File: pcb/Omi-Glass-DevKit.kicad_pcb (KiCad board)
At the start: 2 copper layers, 24.4 x 16.5 mm, 12 parts, among them J1 Conn_01x02, J2 Conn_01x02, SW1 SW_Push, U1 NCP163AFCS280T2G, U2 NCP163AFCT180T2G

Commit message: push R0.0 design for V3 glasses
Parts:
- removed the REF** at (0.00, 8.20)
- removed TH1: Thermistor_NTC, Capacitor_THT:C_Disc_D3.0mm_W1.6mm_P2.50mm
- removed U1: NCP163AFCS280T2G, Package_CSP:WLCSP-4_0.64x0.64mm_P0.35mm
- removed U2: NCP163AFCT180T2G, Package_CSP:WLCSP-4_0.64x0.64mm_P0.35mm
- added JP1: Jumper_2_Open, Jumper:SolderJumper-2_P1.3mm_Open_RoundedPad1.0x1.5mm, F.Cu at (14.3, -1.17)
- moved REF** 6.45 mm to (10.7, 2.10)
- moved J2 3.68 mm to (10.4, -4.50), turned to -90 degrees
- moved J1 2.69 mm to (13.4, -7.27)
- moved R1 0.47 mm to (11.3, 5.58)
- moved R2 0.47 mm to (11.3, 6.73)
- turned J3 to 90 degrees
- renumbered J2 to J3
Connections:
- U3 pad 3: unconnected-(U3-D2-Pad3) -> (no net)
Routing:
- net LOAD: track 13.4 -> 18.6 mm
- net POWER: track 4.40 -> 8.50 mm
- net VBAT1: track 6.38 -> 5.50 mm
- net GND: vias 20 -> 18
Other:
- board size 24.4 x 16.5 mm -> 24.4 x 19.5 mm
- board text added: "for Omi Glass v3"
- board text added: "v3-0.0"
- board text removed: "Design by Alex Lynd"
- board text removed: "OMI"
- board text removed: "v0.1"

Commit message: update production files
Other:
- board text removed: "v3-0.0"

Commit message: bump to R0.2 V3
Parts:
- removed JP1: Jumper_2_Open, Jumper:SolderJumper-2_P1.3mm_Open_RoundedPad1.0x1.5mm
- SW1: footprint Button_Switch_SMD:SW_SPST_EVQP7C -> Button_Switch_SMD:Panasonic_EVQPUL_EVQPUC
- moved SW1 0.82 mm to (13.2, 8.62), turned to 180 degrees
- moved R2 0.73 mm to (11.2, 6.01)
- moved R1 0.73 mm to (11.2, 4.86)
- turned J3 to -90 degrees
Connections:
- J1 pad 2: VBAT1 -> LOAD
- J3 pad 1: GND -> LOAD
- J3 pad 2: LOAD -> GND
- U3 pad 3: (no net) -> unconnected-(U3-D2-Pad3)
- U3 pad 4: (no net) -> unconnected-(U3-D3-Pad4)
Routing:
- net LOAD: track 18.6 -> 24.4 mm
- net VBAT1: track 5.50 -> 0.00 mm
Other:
- board size 24.4 x 19.5 mm -> 25.5 x 19.5 mm
- board text added: "R0.1_V3"

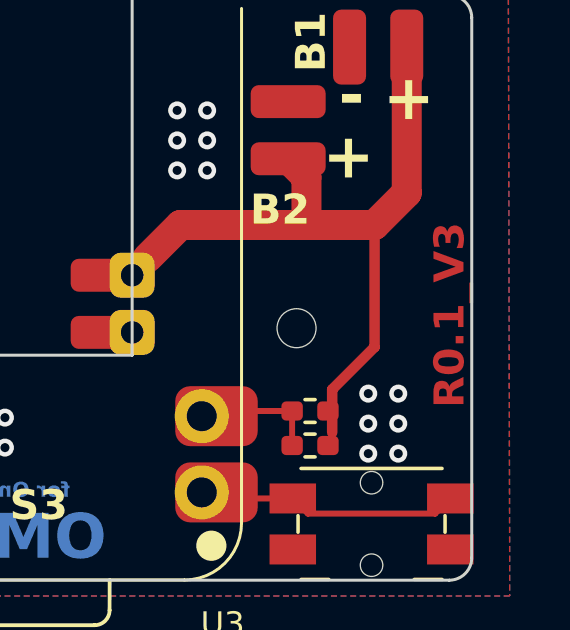
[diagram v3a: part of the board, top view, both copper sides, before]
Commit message: update version on PCB copper
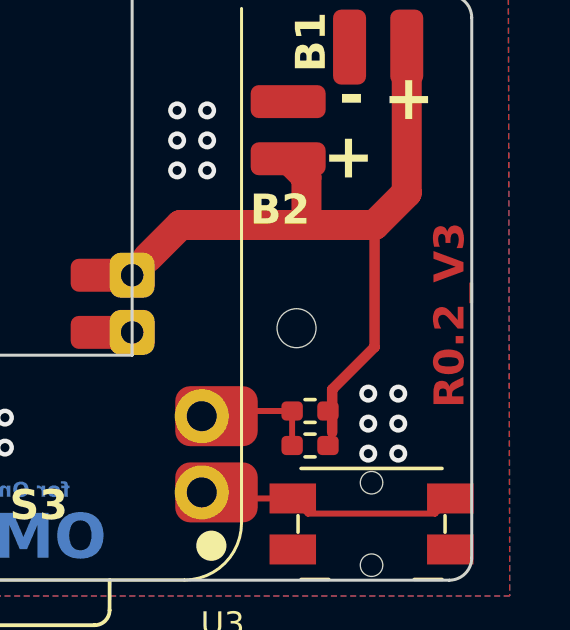
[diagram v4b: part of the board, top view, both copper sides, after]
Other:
- board text added: "R0.2_V3"
- board text removed: "R0.1_V3"
